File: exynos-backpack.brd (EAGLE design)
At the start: 29 x 52 mm, 17 parts, among them IC1 MIC5335-SPYMT, IC2 TXB0108RGY

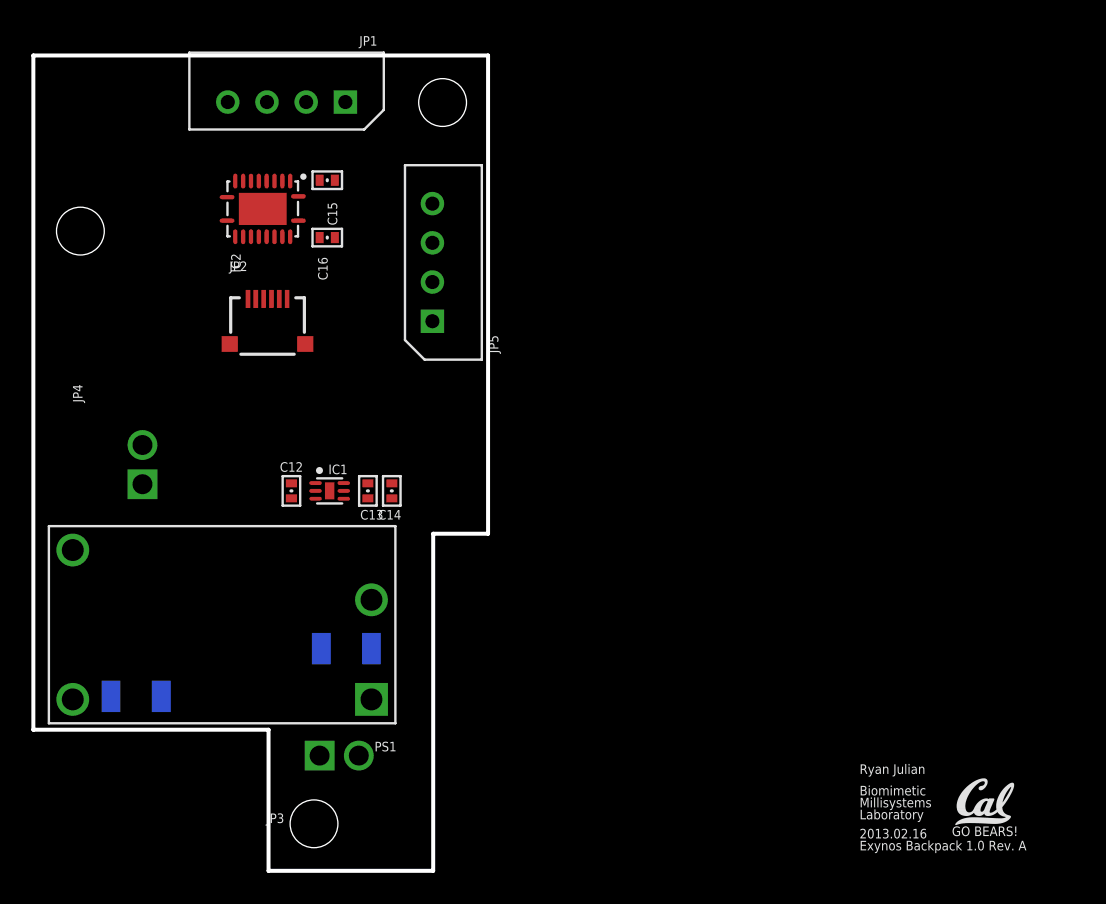
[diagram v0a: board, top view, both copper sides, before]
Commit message: Add hole for encoder cable
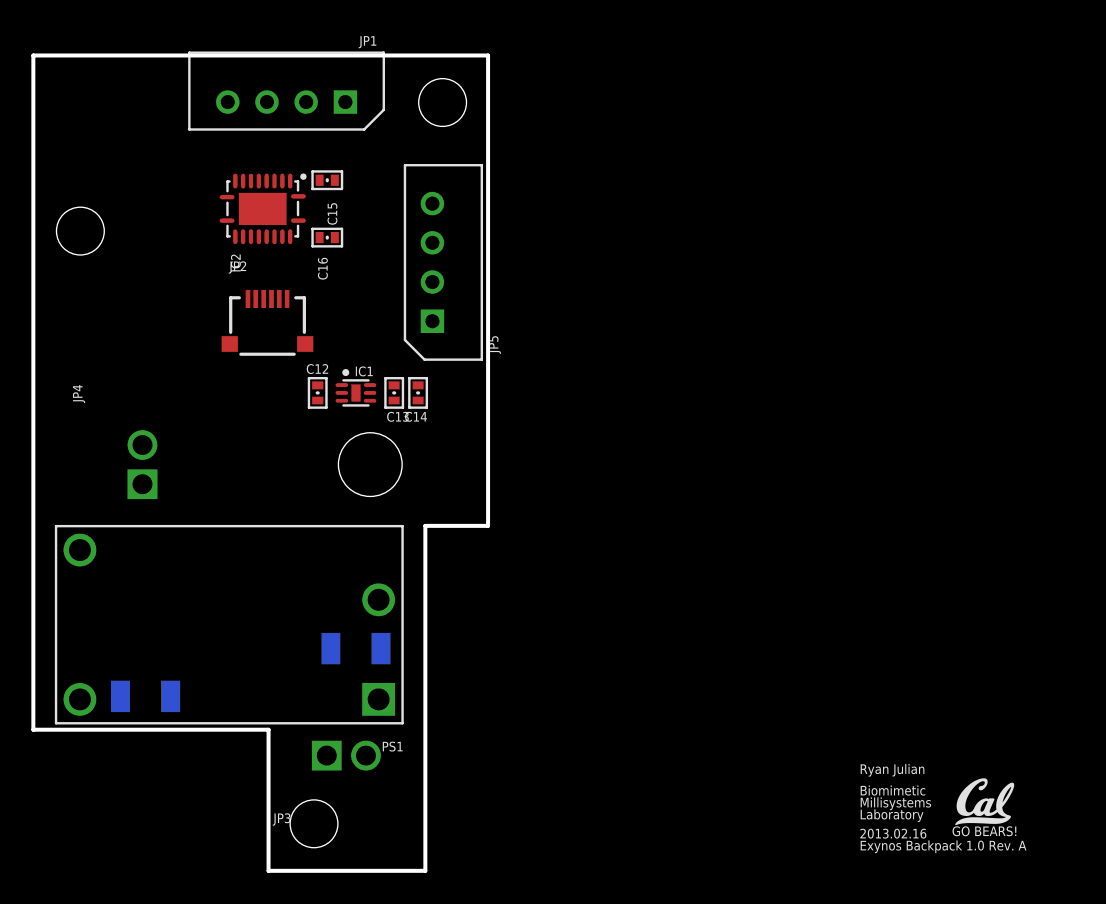
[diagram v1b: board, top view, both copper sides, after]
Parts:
- moved C12 6.47 mm to (18.1, 30.5)
- moved C13 6.47 mm to (23.0, 30.5)
- moved C14 6.47 mm to (24.5, 30.5)
- moved IC1 6.47 mm to (20.6, 30.5)
- moved C10 0.61 mm to (20.6, 14.2)
- moved C11 0.61 mm to (7.16, 11.1)
- moved JP3 0.46 mm to (20.0, 0.00)
- moved PS1 0.46 mm to (12.5, 15.7)
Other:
- outline, holes or cut-outs redrawn
